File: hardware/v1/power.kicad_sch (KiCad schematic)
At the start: 26 parts, among them J2 Conn_01x02, J4 USB_C_Receptacle_USB2.0, J8 Conn_01x02, Q1 AO3401A, U1 AMS1117-3.3, U10 SRV05-4, U4 MAX17044G+U, U9 TPS2113APW

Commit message: some hardware designs
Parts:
- removed C21: 4u7, Capacitor_SMD:C_0603_1608Metric, symbol Device:C_Small
- removed C22: 100n, Capacitor_SMD:C_0402_1005Metric, symbol Device:C_Small
- removed J8: Conn_01x02, Connector_JST:JST_PH_B2B-PH-K_1x02_P2.00mm_Vertical, symbol Connector_Generic:Conn_01x02
- removed R1, R19: 5K1, Resistor_SMD:R_0402_1005Metric, symbol Device:R_Small
- removed R11: 1K5, Resistor_SMD:R_0402_1005Metric, symbol Device:R_Small
- removed U4: MAX17044G+U, Package_DFN_QFN:TDFN-8-1EP_3x2mm_P0.5mm_EP1.3x1.4mm, symbol Battery_Management:MAX17044G+U
- added D2: USB_IND, LED_SMD:LED_0603_1608Metric, symbol Device:LED_Small
- added R16: 1K5, Resistor_SMD:R_0402_1005Metric, symbol Device:R_Small
- D2: value STATUS -> EXT_PWR_IND
- R22: footprint Resistor_SMD:R_0603_1608Metric -> Resistor_SMD:R_0402_1005Metric
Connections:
- net GND: now also D2.1 (K)
- net VBUS: now also R16.1
- net at J4.A5 (CC1): now also J4.B5 (CC2), R1.1
- net VSNS: now reaches R23.2, R24.1, U9.3 (VSNS)
- net ILIM: now reaches R22.1, U9.4 (ILIM)
- new net: D2.2 (A), R16.2
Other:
- note removed: "Fuel Gauge"
- note removed: "VCELL connected to battery pack Max 10.0V"
- moved on the sheet: R1, R22

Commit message: Route another?
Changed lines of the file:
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@@
   (junction (at 121.92 25.4) (diameter 0) (color 0 0 0 0)
   )
+  (junction (at 27.305 137.795) (diameter 0) (color 0 0 0 0)
+  )
   (junction (at 34.29 34.925) (diameter 0) (color 0 0 0 0)
   )
@@
   (junction (at 41.275 45.72) (diameter 0) (color 0 0 0 0)
   )
+  (junction (at 27.305 142.875) (diameter 0) (color 0 0 0 0)
+  )
   (junction (at 48.895 34.925) (diameter 0) (color 0 0 0 0)
   )
@@
   )
   (junction (at 160.02 26.67) (diameter 0) (color 0 0 0 0)
+  )
+  (junction (at 27.305 140.335) (diameter 0) (color 0 0 0 0)
   )
   (no_connect (at 116.205 176.53))
@@
     (stroke (width 0) (type default))
   )
+  (wire (pts (xy 27.305 142.875) (xy 27.305 145.415))
+    (stroke (width 0) (type default))
+  )
   (wire (pts (xy 100.33 32.385) (xy 99.06 32.385))
     (stroke (width 0) (type default))
@@
     (stroke (width 0) (type default))
   )
+  (wire (pts (xy 27.305 137.795) (xy 29.21 137.795))
+    (stroke (width 0) (type default))
+  )
   (wire (pts (xy 60.96 157.48) (xy 59.69 157.48))
     (stroke (width 0) (type default))
@@
     (stroke (width 0) (type default))
   )
+  (wire (pts (xy 27.305 135.255) (xy 27.305 137.795))
+    (stroke (width 0) (type default))
+  )
   (wire (pts (xy 59.69 157.48) (xy 59.69 155.575))
     (stroke (width 0) (type default))
   )
+  (wire (pts (xy 27.305 142.875) (xy 29.21 142.875))
+    (stroke (width 0) (type default))
+  )
   (wire (pts (xy 151.765 37.465) (xy 160.02 37.465))
     (stroke (width 0) (type default))
@@
     (stroke (width 0) (type default))
   )
+  (wire (pts (xy 27.305 137.795) (xy 27.305 140.335))
+    (stroke (width 0) (type default))
+  )
   (wire (pts (xy 160.02 37.465) (xy 160.02 26.67))
     (stroke (width 0) (type default))
@@
     (stroke (width 0) (type default))
   )
+  (wire (pts (xy 29.21 135.255) (xy 27.305 135.255))
+    (stroke (width 0) (type default))
+  )
   (wire (pts (xy 175.26 45.085) (xy 200.025 45.085))
     (stroke (width 0) (type default))
@@
     (stroke (width 0) (type default))
   )
-  (wire (pts (xy 27.305 140.335) (xy 27.305 145.415))
-    (stroke (width 0) (type default))
-  )
+  (wire (pts (xy 27.305 140.335) (xy 27.305 142.875))
+    (stroke (width 0) (type default))
+  )

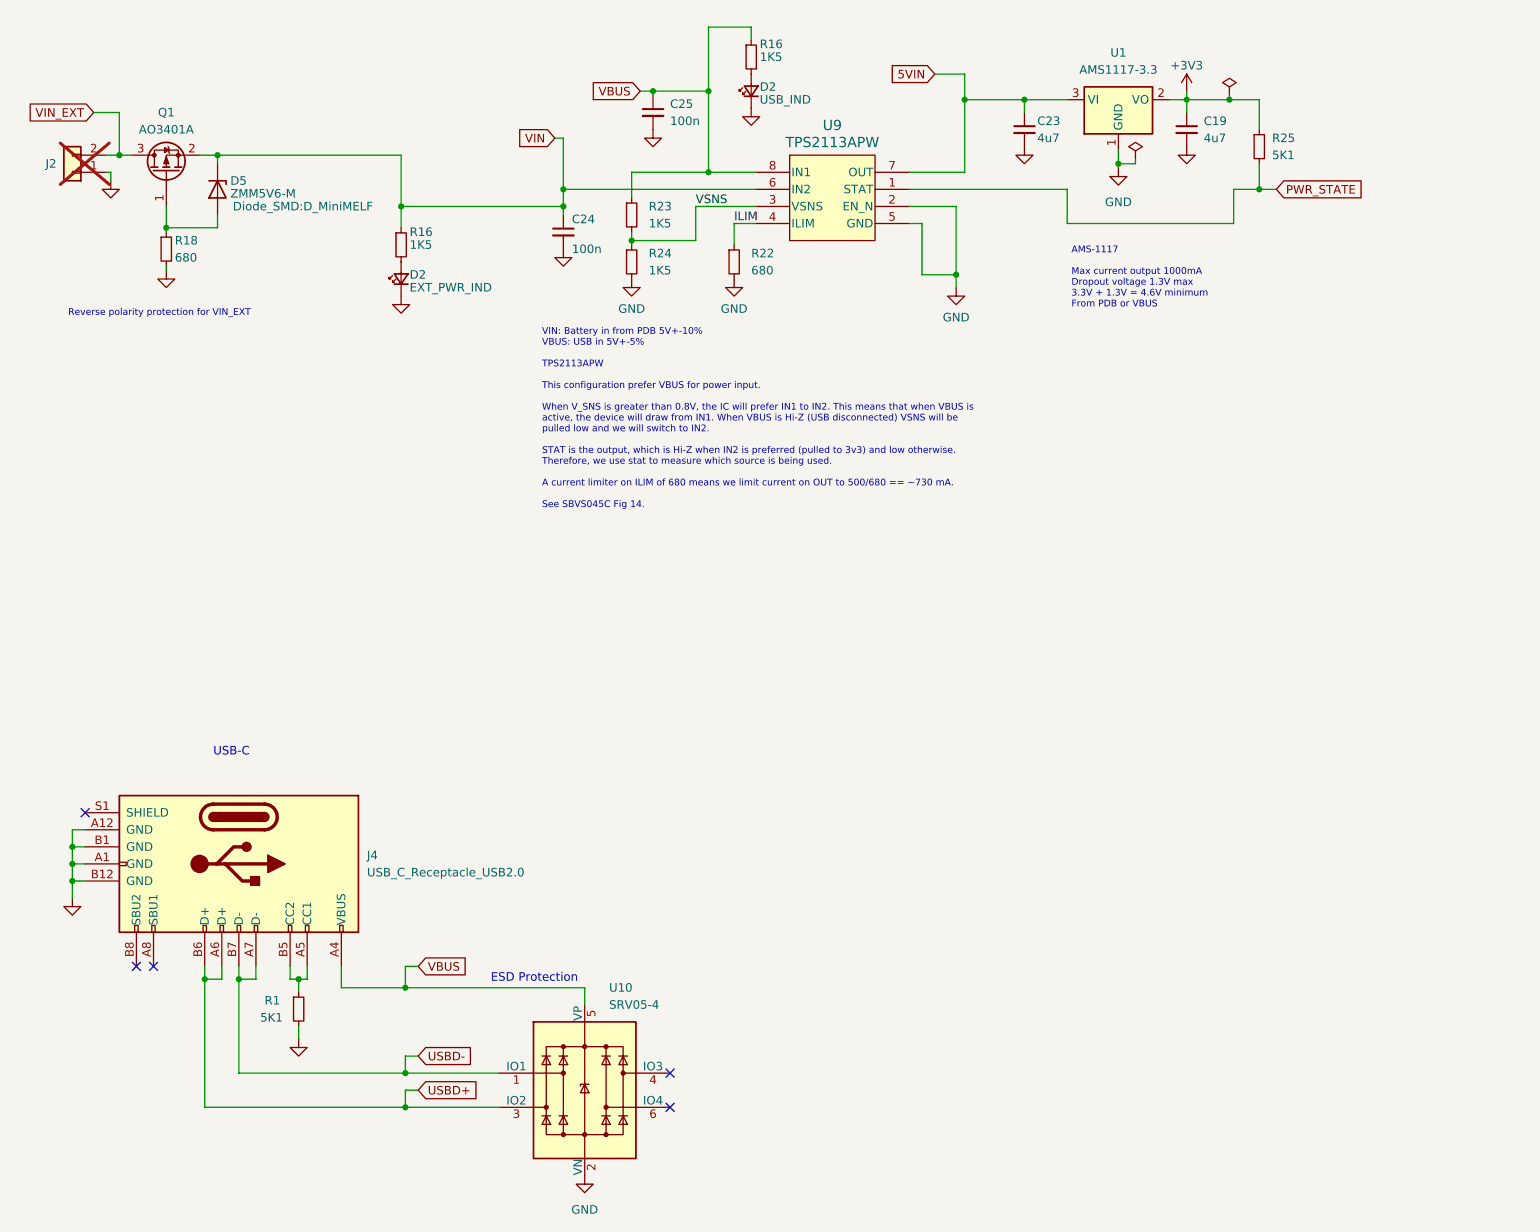
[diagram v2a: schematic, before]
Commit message: JLC part footprints
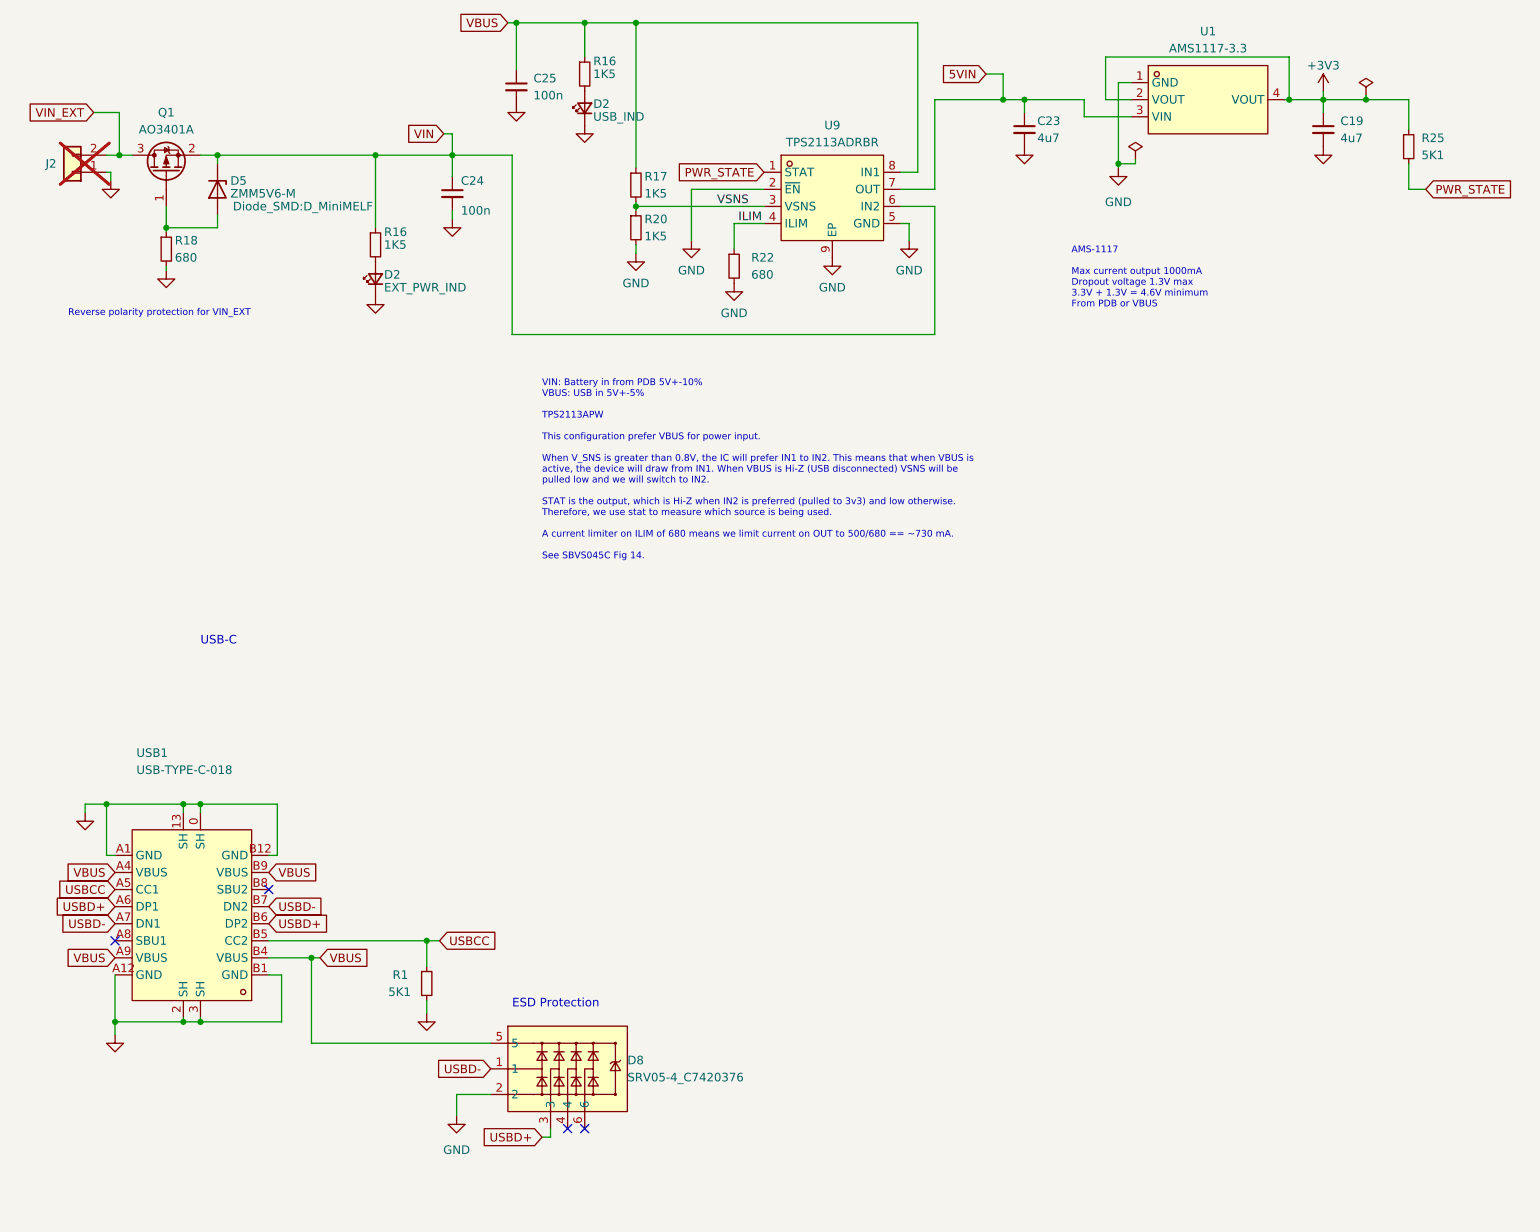
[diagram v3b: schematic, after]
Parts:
- removed J4: USB_C_Receptacle_USB2.0, Connector_USB:USB_C_Receptacle_G-Switch_GT-USB-7010ASV, symbol Connector:USB_C_Receptacle_USB2.0
- removed R23, R24: 1K5, Resistor_SMD:R_0402_1005Metric, symbol Device:R_Small
- removed U1: AMS1117-3.3, Package_TO_SOT_SMD:SOT-223-3_TabPin2, symbol Regulator_Linear:AMS1117-3.3
- removed U10: SRV05-4, Package_TO_SOT_SMD:SOT-23-6, symbol Power_Protection:SRV05-4
- removed U9: TPS2113APW, Package_SO:TSSOP-8_4.4x3mm_P0.65mm, symbol Power_Supervisor:TPS2113APW
- added D8: SRV05-4_C7420376, ofc_sym:SOT-23-6_L2.9-W1.6-P0.95-LS2.8-BL-1, symbol ofc_sym:SRV05-4_C7420376
- added R17, R20: 1K5, Resistor_SMD:R_0402_1005Metric, symbol Device:R_Small
- added U1: AMS1117-3.3, ofc_sym:SOT-223-3_L6.5-W3.4-P2.30-LS7.0-BR, symbol ofc_sym:AMS1117-3.3
- added U9: TPS2113ADRBR, ofc_sym:SON-8_L3.0-W3.0-P0.65-LS3.0-BL-EP, symbol ofc_sym:TPS2113ADRBR
- added USB1: USB-TYPE-C-018, ofc_sym:USB-C_SMD-TYPE-C-31-M-12, symbol ofc_sym:USB-TYPE-C-018
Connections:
- net +3V3: now also U1.2 (VOUT), U1.4 (VOUT)
- net 5VIN: now also U1.3 (VIN), U9.7 (OUT)
- net GND: now also D8.2, R20.2, U1.1 (GND), U9.2 (~{EN}), U9.5 (GND), U9.9 (EP), USB1.0 (SH), USB1.13 (SH), USB1.2 (SH), USB1.3 (SH), USB1.A1 (GND), USB1.A12 (GND), USB1.B1 (GND), USB1.B12 (GND)
- net ILIM: now also U9.4 (ILIM)
- net PWR_STATE: now also U9.1 (STAT)
- net USBD+: now also D8.3, USB1.A6 (DP1), USB1.B6 (DP2)
- net USBD-: now also D8.1, USB1.A7 (DN1), USB1.B7 (DN2)
- net VBUS: now also D8.5, R17.1, U9.8 (IN1), USB1.A4 (VBUS), USB1.A9 (VBUS), USB1.B4 (VBUS), USB1.B9 (VBUS)
- net VIN: now also U9.6 (IN2)
- net VSNS: now also R17.2, R20.1, U9.3 (VSNS)
- net USBCC: now reaches R1.1
- net USBCC: now also USB1.A5 (CC1), USB1.B5 (CC2)
- no-connect marks 5 -> 4
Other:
- moved on the sheet: C19, C24, C25, D2, R1, R16, R22, R25
